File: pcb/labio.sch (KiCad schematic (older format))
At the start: 0 parts

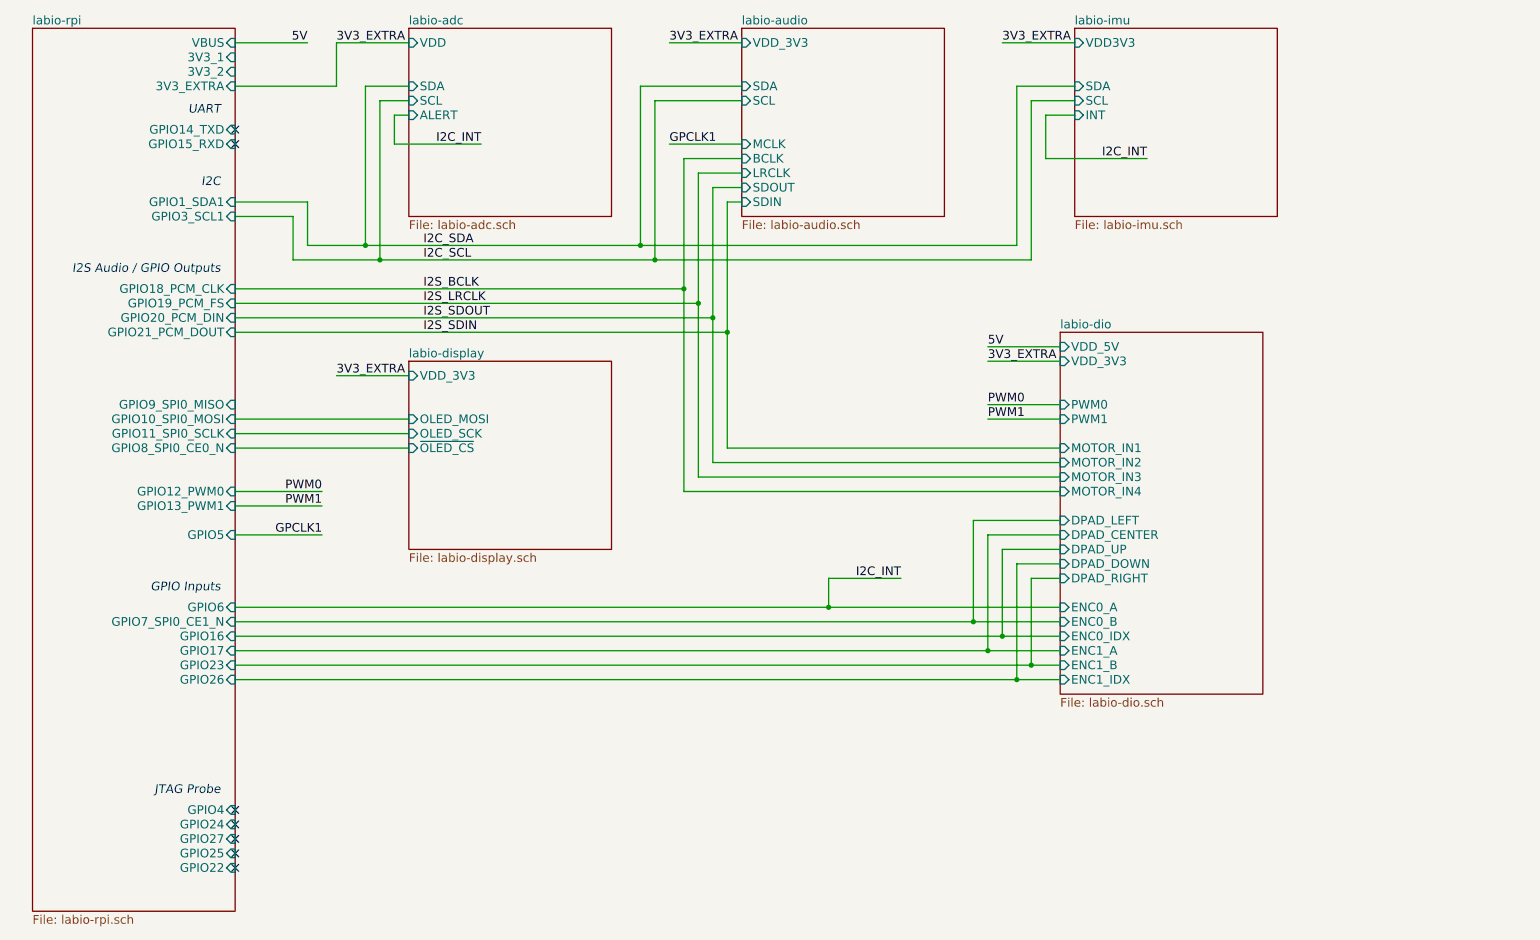
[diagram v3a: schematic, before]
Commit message: add led status indicators, rotary encoder
* add led indicators for motor direction, pwm, encoder (muxed with dpad) pins
* add led indicators for power in all blocks
* split dpad into a different page
* add selectable onboard rotary encoder for testing or user input
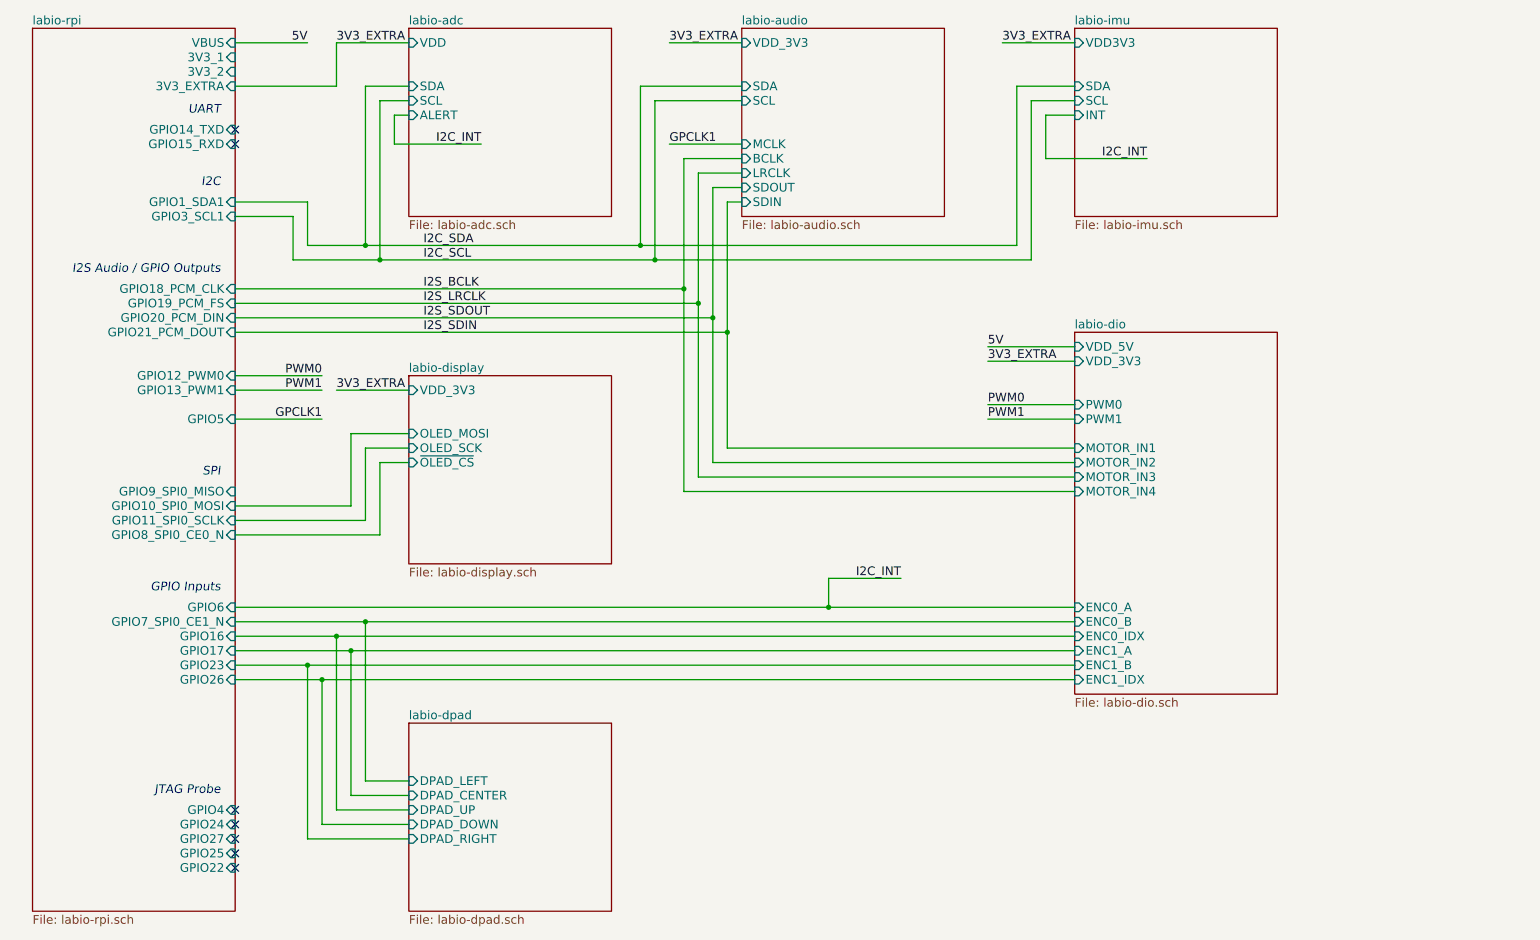
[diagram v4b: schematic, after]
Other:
- note added: "SPI"
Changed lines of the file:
@@
 $Descr A4 11693 8268
 encoding utf-8
-Sheet 1 7
+Sheet 1 8
 Title ""
 Date ""
@@
 F4 "GPIO27" I R 2500 6600 60
 F5 "GPIO22" I R 2500 6800 60
-F6 "GPIO10_SPI0_MOSI" I R 2500 3700 60
-F7 "GPIO9_SPI0_MISO" I R 2500 3600 60
+F6 "GPIO10_SPI0_MOSI" I R 2500 4300 60
+F7 "GPIO9_SPI0_MISO" I R 2500 4200 60
 F8 "3V3_2" I R 2500 1300 60
-F9 "GPIO11_SPI0_SCLK" I R 2500 3800 60
-F10 "GPIO5" I R 2500 4500 60
+F9 "GPIO11_SPI0_SCLK" I R 2500 4400 60
+F10 "GPIO5" I R 2500 3700 60
 F11 "GPIO6" I R 2500 5000 60
 F12 "GPIO26" I R 2500 5500 60
@@
 F17 "GPIO24" I R 2500 6500 60
 F18 "GPIO25" I R 2500 6700 60
-F19 "GPIO8_SPI0_CE0_N" I R 2500 3900 60
+F19 "GPIO8_SPI0_CE0_N" I R 2500 4500 60
 F20 "GPIO7_SPI0_CE1_N" I R 2500 5100 60
 F21 "GPIO1_SDA1" I R 2500 2200 60
 F22 "GPIO3_SCL1" I R 2500 2300 60
 F23 "GPIO17" I R 2500 5300 60
-F24 "GPIO13_PWM1" I R 2500 4300 60
+F24 "GPIO13_PWM1" I R 2500 3500 60
 F25 "GPIO19_PCM_FS" I R 2500 2900 60
 F26 "GPIO18_PCM_CLK" I R 2500 2800 60
-F27 "GPIO12_PWM0" I R 2500 4200 60
+F27 "GPIO12_PWM0" I R 2500 3400 60
 F28 "GPIO16" I R 2500 5200 60
 F29 "GPIO20_PCM_DIN" I R 2500 3000 60
@@
 $EndSheet
 $Sheet
-S 3700 3300 1400 1300
+S 3700 3400 1400 1300
 U 57483FA2
 F0 "labio-display" 60
 F1 "labio-display.sch" 60
-F2 "VDD_3V3" I L 3700 3400 60
-F3 "~OLED_CS" I L 3700 3900 60
-F4 "OLED_SCK" I L 3700 3800 60
-F5 "OLED_MOSI" I L 3700 3700 60
+F2 "VDD_3V3" I L 3700 3500 60
+F3 "~OLED_CS" I L 3700 4000 60
+F4 "OLED_SCK" I L 3700 3900 60
+F5 "OLED_MOSI" I L 3700 3800 60
 $EndSheet
 $Sheet
@@
 $EndSheet
 $Sheet
-S 8200 3100 1400 2500
+S 8300 3100 1400 2500
 U 57484262
 F0 "labio-dio" 60
 F1 "labio-dio.sch" 60
-F2 "DPAD_LEFT" I L 8200 4400 60
-F3 "DPAD_CENTER" I L 8200 4500 60
-F4 "DPAD_UP" I L 8200 4600 60
-F5 "DPAD_DOWN" I L 8200 4700 60
-F6 "DPAD_RIGHT" I L 8200 4800 60
-F7 "VDD_3V3" I L 8200 3300 60
-F8 "PWM0" I L 8200 3600 60
-F9 "PWM1" I L 8200 3700 60
-F10 "MOTOR_IN4" I L 8200 4200 60
-F11 "MOTOR_IN2" I L 8200 4000 60
-F12 "MOTOR_IN3" I L 8200 4100 60
-F13 "MOTOR_IN1" I L 8200 3900 60
-F14 "VDD_5V" I L 8200 3200 60
-F15 "ENC1_A" I L 8200 5300 60
-F16 "ENC1_B" I L 8200 5400 60
-F17 "ENC1_IDX" I L 8200 5500 60
-F18 "ENC0_A" I L 8200 5000 60
-F19 "ENC0_B" I L 8200 5100 60
-F20 "ENC0_IDX" I L 8200 5200 60
-$EndSheet
-Wire Wire Line
-	2500 5500 8200 5500
-Wire Wire Line
-	2500 5400 8200 5400
-Wire Wire Line
-	2500 5300 8200 5300
-Wire Wire Line
-	2500 5200 8200 5200
-Wire Wire Line
-	2500 5100 8200 5100
-Wire Wire Line
-	2500 5000 8200 5000
+F2 "VDD_3V3" I L 8300 3300 60
+F3 "PWM0" I L 8300 3600 60
+F4 "PWM1" I L 8300 3700 60
+F5 "MOTOR_IN4" I L 8300 4200 60
+F6 "MOTOR_IN2" I L 8300 4000 60
+F7 "MOTOR_IN3" I L 8300 4100 60
+F8 "MOTOR_IN1" I L 8300 3900 60
+F9 "VDD_5V" I L 8300 3200 60
+F10 "ENC1_A" I L 8300 5300 60
+F11 "ENC1_B" I L 8300 5400 60
+F12 "ENC1_IDX" I L 8300 5500 60
+F13 "ENC0_A" I L 8300 5000 60
+F14 "ENC0_B" I L 8300 5100 60
+F15 "ENC0_IDX" I L 8300 5200 60
+$EndSheet
+Wire Wire Line
+	2500 5500 8300 5500
+Wire Wire Line
+	2500 5400 8300 5400
+Wire Wire Line
+	2500 5300 8300 5300
+Wire Wire Line
+	2500 5200 8300 5200
+Wire Wire Line
+	2500 5100 8300 5100
+Wire Wire Line
+	2500 5000 8300 5000
 Wire Wire Line
 	2500 1400 3200 1400
@@
 	5500 1800 6000 1800
 Wire Wire Line
-	3200 3400 3700 3400
-Wire Wire Line
-	3700 3700 2500 3700
-Wire Wire Line
-	2500 3900 3700 3900
-Wire Wire Line
-	3700 3800 2500 3800
-Wire Wire Line
-	8200 4700 7900 4700
-Wire Wire Line
-	7900 4700 7900 5500
-Connection ~ 7900 5500
-Wire Wire Line
-	8200 4600 7800 4600
-Wire Wire Line
-	7800 4600 7800 5200
-Connection ~ 7800 5200
-Wire Wire Line
-	8200 4800 8000 4800
-Wire Wire Line
-	8000 4800 8000 5400
-Connection ~ 8000 5400
-Wire Wire Line
-	8200 4500 7700 4500
-Wire Wire Line
-	7700 4500 7700 5300
-Connection ~ 7700 5300
-Wire Wire Line
-	8200 4400 7600 4400
-Wire Wire Line
-	7600 4400 7600 5100
-Connection ~ 7600 5100
+	3200 3500 3700 3500
 Wire Wire Line
 	8300 1600 8100 1600
 Wire Wire Line
-	7700 3300 8200 3300
-Wire Wire Line
-	2500 4200 3100 4200
-Wire Wire Line
-	3100 4300 2500 4300
-Wire Wire Line
-	8200 3600 7700 3600
-Wire Wire Line
-	7700 3700 8200 3700
+	7700 3300 8300 3300
+Wire Wire Line
+	2500 3400 3100 3400
+Wire Wire Line
+	3100 3500 2500 3500
+Wire Wire Line
+	8300 3600 7700 3600
+Wire Wire Line
+	7700 3700 8300 3700
 Text Label 7700 3600 0    60   ~ 0
 PWM0
 Text Label 7700 3700 0    60   ~ 0
 PWM1
-Text Label 3100 4200 2    60   ~ 0
+Text Label 3100 3400 2    60   ~ 0
 PWM0
-Text Label 3100 4300 2    60   ~ 0
+Text Label 3100 3500 2    60   ~ 0
 PWM1
 Text Label 7800 1100 0    60   ~ 0
@@
 3V3_EXTRA
 Wire Wire Line
-	8200 3200 7700 3200
+	8300 3200 7700 3200
 Text Label 7700 3200 0    60   ~ 0
 5V
@@
 GPCLK1
 Wire Wire Line
-	2500 4500 3100 4500
-Text Label 3100 4500 2    60   ~ 0
+	2500 3700 3100 3700
+Text Label 3100 3700 2    60   ~ 0
 GPCLK1
-Text Label 3200 3400 0    60   ~ 0
+Text Label 3200 3500 0    60   ~ 0
 3V3_EXTRA
 Wire Wire Line
@@
 I2S_SDIN
 Wire Wire Line
-	5900 3900 8200 3900
+	5900 3900 8300 3900
 Connection ~ 5900 3100
 Wire Wire Line
-	5800 4000 8200 4000
+	5800 4000 8300 4000
 Connection ~ 5800 3000
 Wire Wire Line
-	5700 4100 8200 4100
+	5700 4100 8300 4100
 Connection ~ 5700 2900
 Wire Wire Line
-	5600 4200 8200 4200
+	5600 4200 8300 4200
 Connection ~ 5600 2800
 Text Notes 2400 4900 2    60   Italic 0
@@
 NoConn ~ 2500 1800
 NoConn ~ 2500 1700
+$Sheet
+S 3700 5800 1400 1300
+U 576EC986
+F0 "labio-dpad" 60
+F1 "labio-dpad.sch" 60
+F2 "DPAD_LEFT" I L 3700 6200 60
+F3 "DPAD_CENTER" I L 3700 6300 60
+F4 "DPAD_UP" I L 3700 6400 60
+F5 "DPAD_DOWN" I L 3700 6500 60
+F6 "DPAD_RIGHT" I L 3700 6600 60
+$EndSheet
+Wire Wire Line
+	3700 6200 3400 6200
+Wire Wire Line
+	3400 6200 3400 5100
+Connection ~ 3400 5100
+Wire Wire Line
+	3700 6300 3300 6300
+Wire Wire Line
+	3300 6300 3300 5300
+Connection ~ 3300 5300
+Wire Wire Line
+	3700 6400 3200 6400
+Wire Wire Line
+	3200 6400 3200 5200
+Connection ~ 3200 5200
+Wire Wire Line
+	3700 6500 3100 6500
+Wire Wire Line
+	3100 6500 3100 5500
+Connection ~ 3100 5500
+Wire Wire Line
+	3700 6600 3000 6600
+Wire Wire Line
+	3000 6600 3000 5400
+Connection ~ 3000 5400
+Wire Wire Line
+	2500 4500 3500 4500
+Wire Wire Line
+	3500 4500 3500 4000
+Wire Wire Line
+	3500 4000 3700 4000
+Wire Wire Line
+	3700 3900 3400 3900
+Wire Wire Line
+	3400 3900 3400 4400
+Wire Wire Line
+	3400 4400 2500 4400
+Wire Wire Line
+	2500 4300 3300 4300
+Wire Wire Line
+	3300 4300 3300 3800
+Wire Wire Line
+	3300 3800 3700 3800
+Text Notes 2400 4100 2    60   Italic 0
+SPI
 $EndSCHEMATC

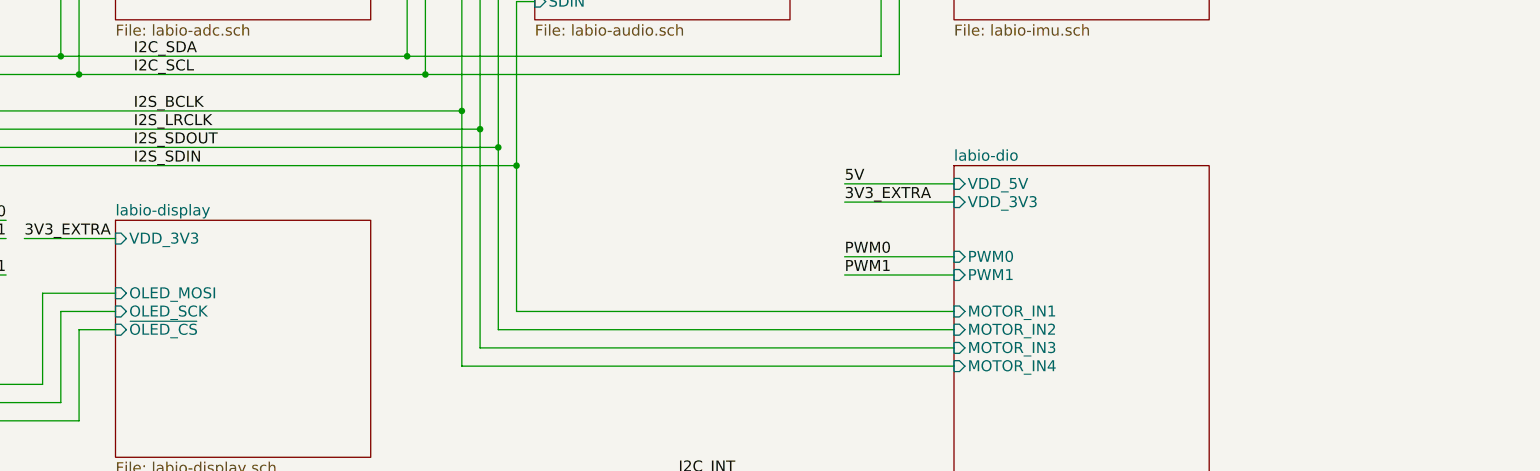
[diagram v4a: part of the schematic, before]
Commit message: make extra footprints. start floorplan. fix display nets. add power expansion header.
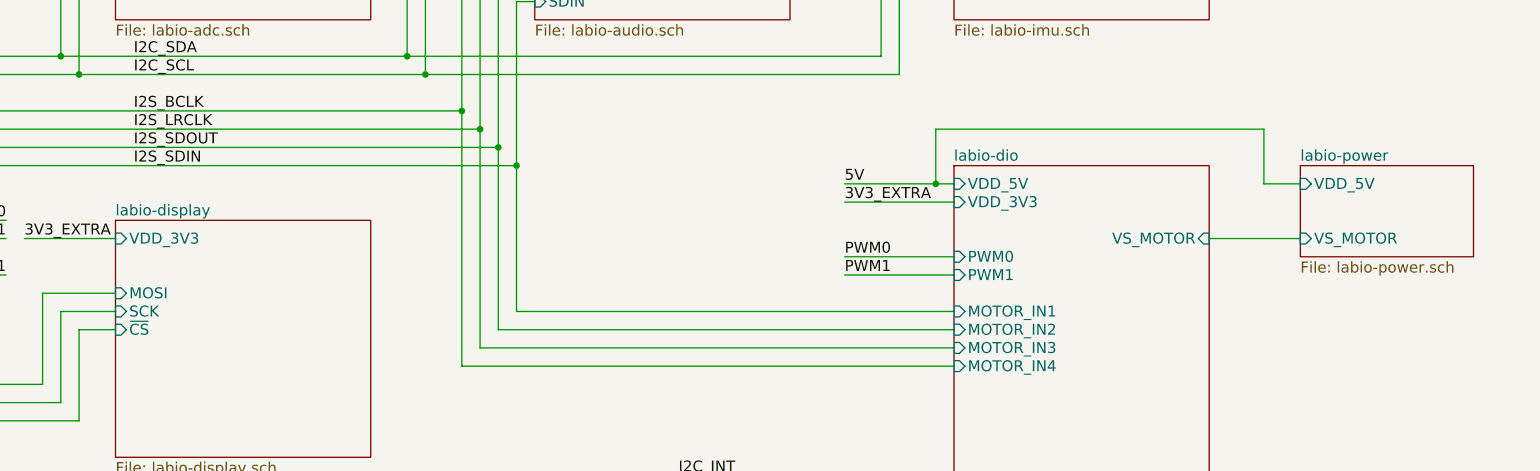
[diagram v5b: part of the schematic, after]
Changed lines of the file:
@@
 $Descr A4 11693 8268
 encoding utf-8
-Sheet 1 8
+Sheet 1 9
 Title ""
 Date ""
@@
 F1 "labio-display.sch" 60
 F2 "VDD_3V3" I L 3700 3500 60
-F3 "~OLED_CS" I L 3700 4000 60
-F4 "OLED_SCK" I L 3700 3900 60
-F5 "OLED_MOSI" I L 3700 3800 60
+F3 "~CS" I L 3700 4000 60
+F4 "SCK" I L 3700 3900 60
+F5 "MOSI" I L 3700 3800 60
 $EndSheet
 $Sheet
@@
 F14 "ENC0_B" I L 8300 5100 60
 F15 "ENC0_IDX" I L 8300 5200 60
+F16 "VS_MOTOR" I R 9700 3500 60
 $EndSheet
 Wire Wire Line
@@
 Text Notes 2400 4100 2    60   Italic 0
 SPI
+$Sheet
+S 10200 3100 950  500
+U 57782573
+F0 "labio-power" 60
+F1 "labio-power.sch" 60
+F2 "VDD_5V" I L 10200 3200 60
+F3 "VS_MOTOR" I L 10200 3500 60
+$EndSheet
+Wire Wire Line
+	10200 3200 10000 3200
+Wire Wire Line
+	10000 3200 10000 2900
+Wire Wire Line
+	10000 2900 8200 2900
+Wire Wire Line
+	8200 2900 8200 3200
+Connection ~ 8200 3200
+Wire Wire Line
+	9700 3500 10200 3500
 $EndSCHEMATC

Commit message: first pass routing, fixed audio header 3v3 net
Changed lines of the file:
@@
 F7 "SDIN" I L 6000 2200 60
 F8 "SDOUT" I L 6000 2100 60
-F9 "VDD_3V3" I L 6000 1100 60
+F9 "VDD3V3" I L 6000 1100 60
 $EndSheet
 NoConn ~ 2500 6800

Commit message: finish rerouting for new parts
* fix adc power supply nets
* redo adc layout
* move motor controller up to make space for headers
* add motor controller heatsink mount
* fix motor controller ground pad net

todo:
* silkscreen
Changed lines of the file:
@@
 $Descr A4 11693 8268
 encoding utf-8
-Sheet 1 9
+Sheet 1 10
 Title ""
 Date ""
@@
 F0 "labio-adc" 60
 F1 "labio-adc.sch" 60
-F2 "VDD" I L 3700 1100 60
-F3 "SDA" I L 3700 1400 60
-F4 "SCL" I L 3700 1500 60
-F5 "ALERT" I L 3700 1600 60
+F2 "SDA" I L 3700 1400 60
+F3 "SCL" I L 3700 1500 60
+F4 "ALERT" I L 3700 1600 60
+F5 "VDD5V" I L 3700 1100 60
+F6 "VDD3V3" I L 3700 1200 60
 $EndSheet
 $Sheet
@@
 	2500 5000 8300 5000
 Wire Wire Line
-	2500 1400 3200 1400
+	2500 1400 3100 1400
 Wire Wire Line
 	7800 1100 8300 1100
-Wire Wire Line
-	3700 1100 3200 1100
 Wire Wire Line
 	2500 2200 3000 2200
@@
 3V3_EXTRA
 Wire Wire Line
-	8300 3200 7700 3200
+	7700 3200 8300 3200
 Text Label 7700 3200 0    60   ~ 0
 5V
@@
 Text Label 3200 3500 0    60   ~ 0
 3V3_EXTRA
-Wire Wire Line
-	3200 1100 3200 1400
-Text Label 3200 1100 0    60   ~ 0
-3V3_EXTRA
-Wire Wire Line
-	2500 1100 3000 1100
+Text Label 3000 1400 2    60   ~ 0
+3V3_EXTRA
+Wire Wire Line
+	2500 1100 3700 1100
 Text Label 3000 1100 2    60   ~ 0
 5V
@@
 Wire Wire Line
 	9700 3500 10200 3500
+Wire Wire Line
+	3100 1400 3100 1200
+Wire Wire Line
+	3100 1200 3700 1200
+$Sheet
+S 10200 5100 950  500
+U 578DDEC2
+F0 "labio-mech" 60
+F1 "labio-mech.sch" 60
+$EndSheet
 $EndSCHEMATC
